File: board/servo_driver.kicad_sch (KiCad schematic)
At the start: 0 parts

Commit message: Hopefully finished schema for pcb
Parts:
- added C2: 33uF, CAP-8*11.5, symbol SCH_Buck Converter_2023-10-10:C_FBF4E86A
- added R10, R11, R12, R13, R14, R15, R16, R17, R18, R19, R20, R21, R22, R7, R8, R9: 220, symbol Device:R
- added R5: 10k, symbol Device:R
- added U5: PCA9685PW, Package_SO:TSSOP-28_4.4x9.7mm_P0.65mm, symbol Driver_LED:PCA9685PW
- added conn_3x1, conn_3x2, conn_3x3, conn_3x4: conn_03x04_Pin, symbol .kicad_sym:conn_03x04_Pin
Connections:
- new net: R5.2, U5.23 (~{OE})
- new net: R11.1, conn_3x2. (9)
- new net: R13.1, conn_3x2. (9)
- new net: R10.1, conn_3x1. (9)
- new net: R21.1, conn_3x4. (9)
- new net: R9.1, conn_3x1. (9)
- new net: R15.1, conn_3x3. (9)
- new net: R18.1, conn_3x3. (9)
- new net: R14.1, conn_3x2. (9)
- new net: R16.1, conn_3x3. (9)
- new net: R17.1, conn_3x3. (9)
- new net: R7.1, conn_3x1. (9)
- new net: R8.1, conn_3x1. (9)
- new net: R22.1, conn_3x4. (9)
- new net: R20.1, conn_3x4. (9)
- new net: R19.1, conn_3x4. (9)
- new net: R12.1, conn_3x2. (9)
- new net +5V: C2.1, U5.1 (A0), U5.24 (A5), U5.28 (VDD), U5.3 (A2), U5.4 (A3), conn_3x1. (9), conn_3x2. (9), conn_3x3. (9)
- new net GND: C2.2, R5.1, U5.2 (A1), U5.25 (EXTCLK), U5.5 (A4), conn_3x1. (9), conn_3x2. (9), conn_3x3. (9), conn_3x4. (9)
- new net PWM0: R14.2, R7.2, U5.6 (LED0)
- new net PWM1: R8.2, U5.7 (LED1)
- new net PWM10: R17.2, U5.17 (LED10)
- new net PWM11: R18.2, U5.18 (LED11)
- new net PWM12: R19.2, U5.19 (LED12)
- new net PWM13: R20.2, U5.20 (LED13)
- new net PWM14: R21.2, U5.21 (LED14)
- new net PWM15: R22.2, U5.22 (LED15)
- new net PWM2: R9.2, U5.8 (LED2)
- new net PWM3: R10.2, U5.9 (LED3)
- new net PWM4: R11.2, U5.10 (LED4)
- new net PWM5: R12.2, U5.11 (LED5)
- new net PWM6: U5.12 (LED6)
- new net PWM7: R13.2, U5.13 (LED7)
- new net PWM8: R15.2, U5.15 (LED8)
- new net PWM9: R16.2, U5.16 (LED9)
- new net SDA: U5.27 (SDA)
- new net SLC: U5.26 (SCL)
- no-connect marks 0 -> 5
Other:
- note added: "PCA9685"
- note added: "Pinout"

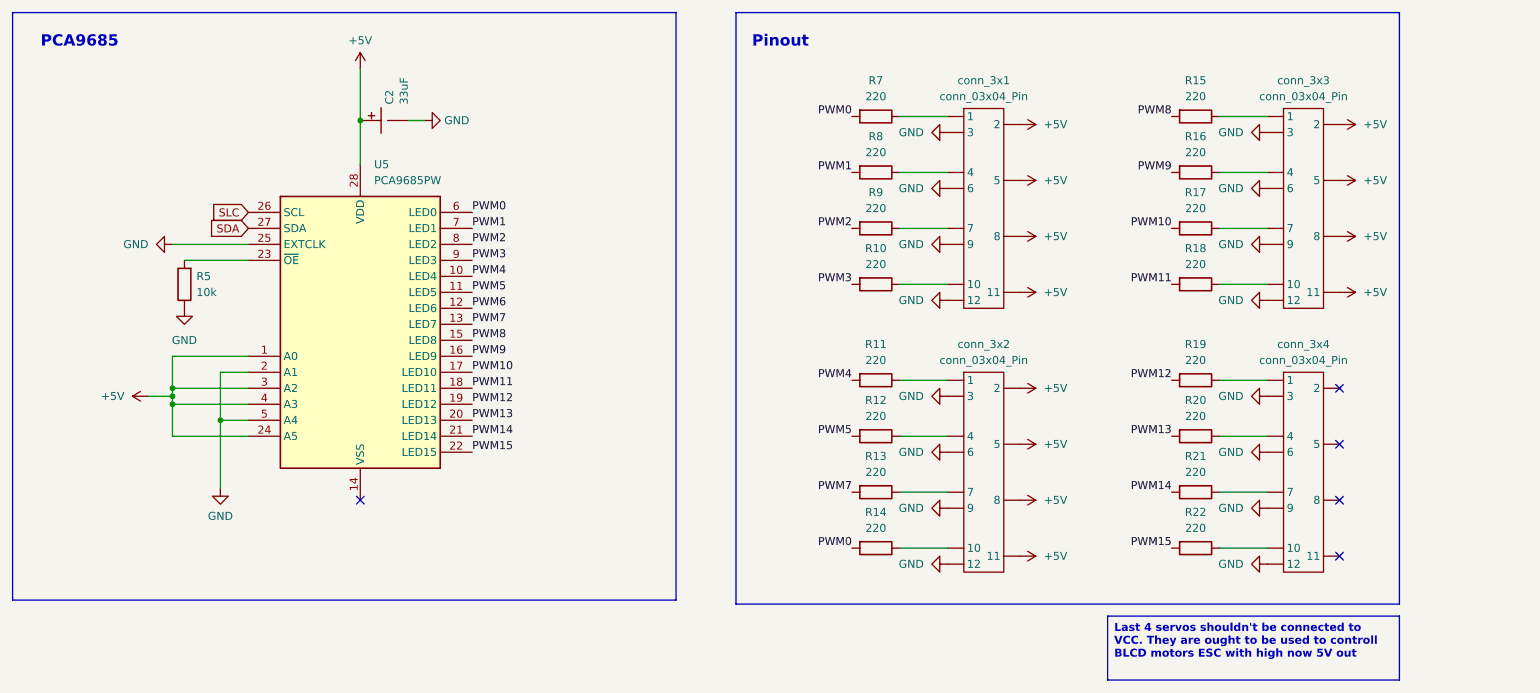
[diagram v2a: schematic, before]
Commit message: Updated schme to comply with electrical rules checker, prepared sensor logic for rewrite
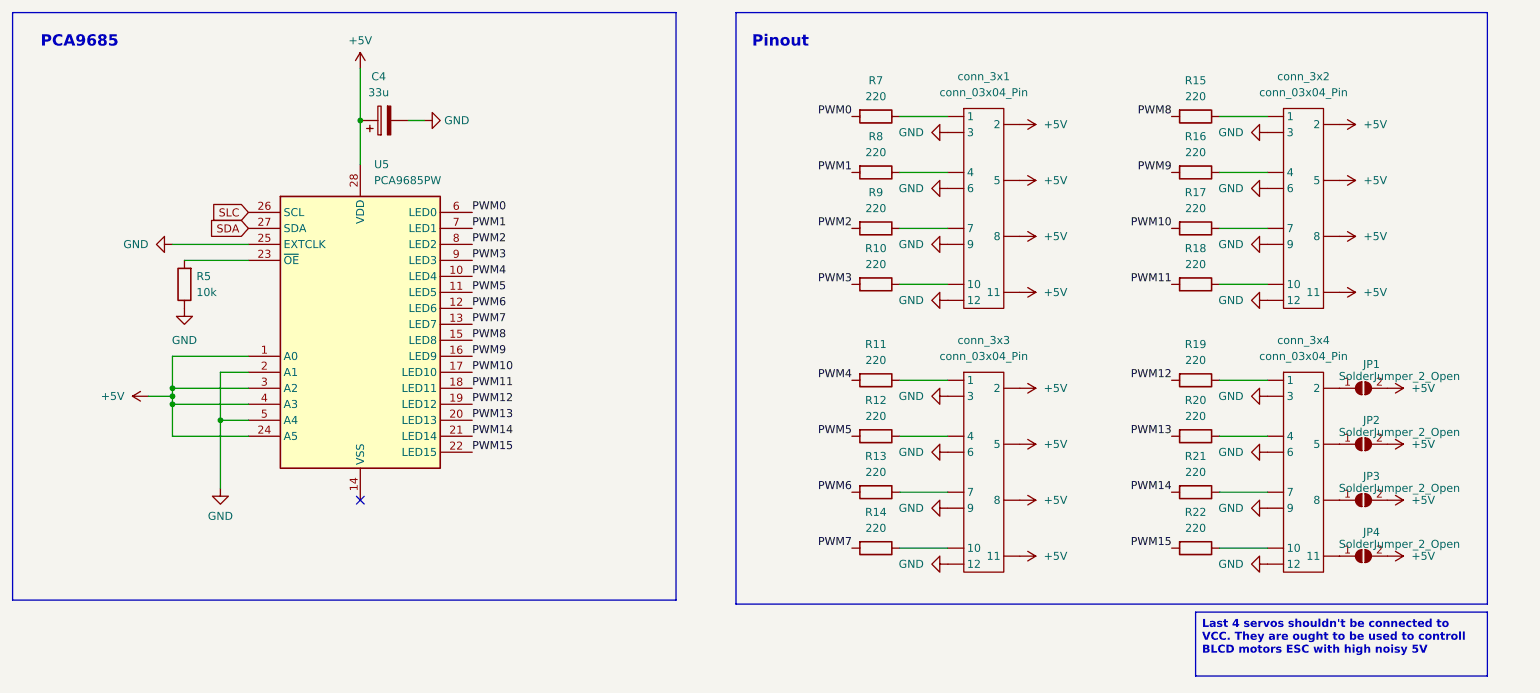
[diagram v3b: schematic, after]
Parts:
- removed C2: 33uF, CAP-8*11.5, symbol SCH_Buck Converter_2023-10-10:C_FBF4E86A
- removed conn_3x1, conn_3x2, conn_3x3, conn_3x4: conn_03x04_Pin, symbol .kicad_sym:conn_03x04_Pin
- added C4: 33u, symbol Device:C_Polarized
- added JP1, JP2, JP3, JP4: SolderJumper_2_Open, Jumper:SolderJumper-2_P1.3mm_Open_Pad1.0x1.5mm, symbol Jumper:SolderJumper_2_Open
- added conn_3x1, conn_3x2, conn_3x3, conn_3x4: conn_03x04_Pin, Custom_Footprints:PinHeader_3x04, symbol Custom_Symbols:conn_03x04_Pin
- R10, R11, R12, R13, R14, R15, R16, R17, R18, R19, R20, R21, R22, R5, R7, R8, R9: footprint (none) -> Resistor_SMD:R_0603_1608Metric
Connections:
- net +5V: now also C4.1, JP1.2 (B), JP2.2 (B), JP3.2 (B), JP4.2 (B), conn_3x1. (9), conn_3x2. (9), conn_3x3. (9)
- net GND: now also C4.2, conn_3x1. (9), conn_3x2. (9), conn_3x3. (9), conn_3x4. (9)
- net PWM0: no longer R14.2
- net PWM6: now also R13.2
- net PWM7: now also R14.2; no longer R13.2
- net at R11.1: now also conn_3x3. (9)
- net at R13.1: now also conn_3x3. (9)
- net at R10.1: now also conn_3x1. (9)
- net at R21.1: now also conn_3x4. (9)
- net at R9.1: now also conn_3x1. (9)
- net at R15.1: now also conn_3x2. (9)
- net at R18.1: now also conn_3x2. (9)
- net at R14.1: now also conn_3x3. (9)
- net at R16.1: now also conn_3x2. (9)
- net at R17.1: now also conn_3x2. (9)
- net at R7.1: now also conn_3x1. (9)
- net at R8.1: now also conn_3x1. (9)
- net at R22.1: now also conn_3x4. (9)
- net at R20.1: now also conn_3x4. (9)
- net at R19.1: now also conn_3x4. (9)
- net at R12.1: now also conn_3x3. (9)
- new net: JP3.1 (A), conn_3x4. (9)
- new net: JP2.1 (A), conn_3x4. (9)
- new net: JP4.1 (A), conn_3x4. (9)
- new net: JP1.1 (A), conn_3x4. (9)
- no-connect marks 5 -> 1

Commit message: More work in reformating drone side of codebase to be semi usable
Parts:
- C4: footprint (none) -> Capacitor_THT:CP_Radial_D8.0mm_P3.50mm
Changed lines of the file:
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@@
       (effects (font (size 1.27 1.27)))
     )
-    (property "Footprint" "" (at 85.725 65.7098 0)
+    (property "Footprint" "Capacitor_THT:CP_Radial_D8.0mm_P3.50mm" (at 85.725 65.7098 0)
       (effects (font (size 1.27 1.27)) hide)
     )

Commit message: Started work on PCB design, more work on rewritting firmware to be semi usable
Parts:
- C4: footprint Capacitor_THT:CP_Radial_D8.0mm_P3.50mm -> Capacitor_THT:CP_Radial_D5.0mm_P2.50mm
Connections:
- net +5V: now also conn_3x1.11, conn_3x1.2, conn_3x1.5, conn_3x1.8, conn_3x2.11, conn_3x2.2, conn_3x2.5, conn_3x2.8, conn_3x3.11, conn_3x3.2, conn_3x3.5, conn_3x3.8; no longer conn_3x1. (9), conn_3x2. (9), conn_3x3. (9)
- net GND: now also conn_3x1.12, conn_3x1.3, conn_3x1.6, conn_3x1.9, conn_3x2.12, conn_3x2.3, conn_3x2.6, conn_3x2.9, conn_3x3.12, conn_3x3.3, conn_3x3.6, conn_3x3.9, conn_3x4.12, conn_3x4.3, conn_3x4.6, conn_3x4.9; no longer conn_3x1. (9), conn_3x2. (9), conn_3x3. (9), conn_3x4. (9)
- net at R11.1: now also conn_3x3.1; no longer conn_3x3. (9)
- net at JP3.1 (A): now also conn_3x4.8; no longer conn_3x4. (9)
- net at R13.1: now also conn_3x3.7; no longer conn_3x3. (9)
- net at R14.1: now also conn_3x3.10; no longer conn_3x3. (9)
- net at R12.1: now also conn_3x3.4; no longer conn_3x3. (9)
- net at R10.1: now also conn_3x1.10; no longer conn_3x1. (9)
- net at R9.1: now also conn_3x1.7; no longer conn_3x1. (9)
- net at R7.1: now also conn_3x1.1; no longer conn_3x1. (9)
- net at R8.1: now also conn_3x1.4; no longer conn_3x1. (9)
- net at JP2.1 (A): now also conn_3x4.5; no longer conn_3x4. (9)
- net at JP4.1 (A): now also conn_3x4.11; no longer conn_3x4. (9)
- net at R21.1: now also conn_3x4.7; no longer conn_3x4. (9)
- net at R15.1: now also conn_3x2.1; no longer conn_3x2. (9)
- net at R18.1: now also conn_3x2.10; no longer conn_3x2. (9)
- net at JP1.1 (A): now also conn_3x4.2; no longer conn_3x4. (9)
- net at R16.1: now also conn_3x2.4; no longer conn_3x2. (9)
- net at R17.1: now also conn_3x2.7; no longer conn_3x2. (9)
- net at R22.1: now also conn_3x4.10; no longer conn_3x4. (9)
- net at R20.1: now also conn_3x4.4; no longer conn_3x4. (9)
- net at R19.1: now also conn_3x4.1; no longer conn_3x4. (9)
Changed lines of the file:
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@@
+    )
+  )
+  (symbol (lib_name "conn_03x04_Pin_1") (lib_id "Custom_Symbols:conn_03x04_Pin") (at 176.53 62.23 0) (unit 1)
+    (in_bom yes) (on_board yes) (dnp no) (fields_autoplaced)
+    (property "Reference" "conn_3x1" (at 177.165 59.69 0)
+      (effects (font (size 1.27 1.27)))
+    )
+    (property "Value" "conn_03x04_Pin" (at 177.165 62.23 0)
+      (effects (font (size 1.27 1.27)))
+    )
+    (property "Footprint" "Custom_Footprints:PinHeader_3x04" (at 176.53 62.23 0)
+      (effects (font (size 1.27 1.27)) hide)
+    )
+    (property "Datasheet" "" (at 176.53 62.23 0)
+      (effects (font (size 1.27 1.27)) hide)
+    )
+    (pin "1")
+    (pin "10")
+    (pin "11")
+    (pin "12")
+    (pin "2")
+    (pin "3")
+    (pin "4")
+    (pin "5")
+    (pin "6")
+    (pin "7")
+    (pin "8")
+    (pin "9")
+    (instances
+      (project "uav_project"
+        (path "/a8bf0924-b264-4c19-8c7e-9c0e131cacba/46d9e855-1ab1-4192-9cab-93e4258e1e2b"
+          (reference "conn_3x1") (unit 1)
+        )
+      )
     )
   )
@@
     )
   )
-  (symbol (lib_id "Custom_Symbols:conn_03x04_Pin") (at 176.53 104.14 0) (unit 1)
-    (in_bom yes) (on_board yes) (dnp no) (fields_autoplaced)
-    (property "Reference" "conn_3x3" (at 177.165 101.6 0)
-      (effects (font (size 1.27 1.27)))
-    )
-    (property "Value" "conn_03x04_Pin" (at 177.165 104.14 0)
-      (effects (font (size 1.27 1.27)))
-    )
-    (property "Footprint" "Custom_Footprints:PinHeader_3x04" (at 176.53 104.14 0)
-      (effects (font (size 1.27 1.27)) hide)
-    )
-    (property "Datasheet" "" (at 176.53 104.14 0)
-      (effects (font (size 1.27 1.27)) hide)
-    )
-    (pin "")
-    (pin "")
-    (pin "")
-    (pin "")
-    (pin "")
-    (pin "")
-    (pin "")
-    (pin "")
-    (pin "")
-    (pin "")
-    (pin "")
-    (pin "")
-    (instances
-      (project "uav_project"
-        (path "/a8bf0924-b264-4c19-8c7e-9c0e131cacba/46d9e855-1ab1-4192-9cab-93e4258e1e2b"
-          (reference "conn_3x3") (unit 1)
-        )
-      )
-    )
-  )
   (symbol (lib_id "power:+5V") (at 233.68 76.2 270) (unit 1)
     (in_bom yes) (on_board yes) (dnp no) (fields_autoplaced)
@@
     )
   )
-  (symbol (lib_id "Custom_Symbols:conn_03x04_Pin") (at 176.53 62.23 0) (unit 1)
-    (in_bom yes) (on_board yes) (dnp no) (fields_autoplaced)
-    (property "Reference" "conn_3x1" (at 177.165 59.69 0)
-      (effects (font (size 1.27 1.27)))
-    )
-    (property "Value" "conn_03x04_Pin" (at 177.165 62.23 0)
-      (effects (font (size 1.27 1.27)))
-    )
-    (property "Footprint" "Custom_Footprints:PinHeader_3x04" (at 176.53 62.23 0)
-      (effects (font (size 1.27 1.27)) hide)
-    )
-    (property "Datasheet" "" (at 176.53 62.23 0)
-      (effects (font (size 1.27 1.27)) hide)
-    )
-    (pin "")
-    (pin "")
-    (pin "")
-    (pin "")
-    (pin "")
-    (pin "")
-    (pin "")
-    (pin "")
-    (pin "")
-    (pin "")
-    (pin "")
-    (pin "")
-    (instances
-      (project "uav_project"
-        (path "/a8bf0924-b264-4c19-8c7e-9c0e131cacba/46d9e855-1ab1-4192-9cab-93e4258e1e2b"
-          (reference "conn_3x1") (unit 1)
+  (symbol (lib_name "conn_03x04_Pin_1") (lib_id "Custom_Symbols:conn_03x04_Pin") (at 227.33 62.23 0) (unit 1)
+    (in_bom yes) (on_board yes) (dnp no) (fields_autoplaced)
+    (property "Reference" "conn_3x2" (at 227.965 59.69 0)
+      (effects (font (size 1.27 1.27)))
+    )
+    (property "Value" "conn_03x04_Pin" (at 227.965 62.23 0)
+      (effects (font (size 1.27 1.27)))
+    )
+    (property "Footprint" "Custom_Footprints:PinHeader_3x04" (at 227.33 62.23 0)
+      (effects (font (size 1.27 1.27)) hide)
+    )
+    (property "Datasheet" "" (at 227.33 62.23 0)
+      (effects (font (size 1.27 1.27)) hide)
+    )
+    (pin "1")
+    (pin "10")
+    (pin "11")
+    (pin "12")
+    (pin "2")
+    (pin "3")
+    (pin "4")
+    (pin "5")
+    (pin "6")
+    (pin "7")
+    (pin "8")
+    (pin "9")
+    (instances
+      (project "uav_project"
+        (path "/a8bf0924-b264-4c19-8c7e-9c0e131cacba/46d9e855-1ab1-4192-9cab-93e4258e1e2b"
+          (reference "conn_3x2") (unit 1)
         )
       )
@@
     )
   )
+  (symbol (lib_name "conn_03x04_Pin_1") (lib_id "Custom_Symbols:conn_03x04_Pin") (at 227.33 104.14 0) (unit 1)
+    (in_bom yes) (on_board yes) (dnp no) (fields_autoplaced)
+    (property "Reference" "conn_3x4" (at 227.965 101.6 0)
+      (effects (font (size 1.27 1.27)))
+    )
+    (property "Value" "conn_03x04_Pin" (at 227.965 104.14 0)
+      (effects (font (size 1.27 1.27)))
+    )
+    (property "Footprint" "Custom_Footprints:PinHeader_3x04" (at 227.33 104.14 0)
+      (effects (font (size 1.27 1.27)) hide)
+    )
+    (property "Datasheet" "" (at 227.33 104.14 0)
+      (effects (font (size 1.27 1.27)) hide)
+    )
+    (pin "1")
+    (pin "10")
+    (pin "11")
+    (pin "12")
+    (pin "2")
+    (pin "3")
+    (pin "4")
+    (pin "5")
+    (pin "6")
+    (pin "7")
+    (pin "8")
+    (pin "9")
+    (instances
+      (project "uav_project"
+        (path "/a8bf0924-b264-4c19-8c7e-9c0e131cacba/46d9e855-1ab1-4192-9cab-93e4258e1e2b"
+          (reference "conn_3x4") (unit 1)
+        )
+      )
+    )
+  )
   (symbol (lib_id "Device:R") (at 210.82 66.04 270) (unit 1)
     (in_bom yes) (on_board yes) (dnp no) (fields_autoplaced)
@@
     )
   )
+  (symbol (lib_name "conn_03x04_Pin_1") (lib_id "Custom_Symbols:conn_03x04_Pin") (at 176.53 104.14 0) (unit 1)
+    (in_bom yes) (on_board yes) (dnp no) (fields_autoplaced)
+    (property "Reference" "conn_3x3" (at 177.165 101.6 0)
+      (effects (font (size 1.27 1.27)))
+    )
+    (property "Value" "conn_03x04_Pin" (at 177.165 104.14 0)
+      (effects (font (size 1.27 1.27)))
+    )
+    (property "Footprint" "Custom_Footprints:PinHeader_3x04" (at 176.53 104.14 0)
+      (effects (font (size 1.27 1.27)) hide)
+    )
+    (property "Datasheet" "" (at 176.53 104.14 0)
+      (effects (font (size 1.27 1.27)) hide)
+    )
+    (pin "1")
+    (pin "10")
+    (pin "11")
+    (pin "12")
+    (pin "2")
+    (pin "3")
+    (pin "4")
+    (pin "5")
+    (pin "6")
+    (pin "7")
+    (pin "8")
+    (pin "9")
+    (instances
+      (project "uav_project"
+        (path "/a8bf0924-b264-4c19-8c7e-9c0e131cacba/46d9e855-1ab1-4192-9cab-93e4258e1e2b"
+          (reference "conn_3x3") (unit 1)
+        )
+      )
+    )
+  )
   (symbol (lib_id "Device:R") (at 160.02 134.62 270) (unit 1)
     (in_bom yes) (on_board yes) (dnp no) (fields_autoplaced)
@@
     )
   )
-  (symbol (lib_id "Custom_Symbols:conn_03x04_Pin") (at 227.33 62.23 0) (unit 1)
-    (in_bom yes) (on_board yes) (dnp no) (fields_autoplaced)
-    (property "Reference" "conn_3x2" (at 227.965 59.69 0)
-      (effects (font (size 1.27 1.27)))
-    )
-    (property "Value" "conn_03x04_Pin" (at 227.965 62.23 0)
-      (effects (font (size 1.27 1.27)))
-    )
-    (property "Footprint" "Custom_Footprints:PinHeader_3x04" (at 227.33 62.23 0)
-      (effects (font (size 1.27 1.27)) hide)
-    )
-    (property "Datasheet" "" (at 227.33 62.23 0)
-      (effects (font (size 1.27 1.27)) hide)
-    )
-    (pin "")
-    (pin "")
-    (pin "")
-    (pin "")
-    (pin "")
-    (pin "")
-    (pin "")
-    (pin "")
-    (pin "")
-    (pin "")
-    (pin "")
-    (pin "")
-    (instances
-      (project "uav_project"
-        (path "/a8bf0924-b264-4c19-8c7e-9c0e131cacba/46d9e855-1ab1-4192-9cab-93e4258e1e2b"
-          (reference "conn_3x2") (unit 1)
-        )
-      )
-    )
-  )
   (symbol (lib_id "power:+5V") (at 44.45 110.49 90) (unit 1)
     (in_bom yes) (on_board yes) (dnp no) (fields_autoplaced)
@@
       (effects (font (size 1.27 1.27)))
     )
-    (property "Footprint" "Capacitor_THT:CP_Radial_D8.0mm_P3.50mm" (at 85.725 65.7098 0)
+    (property "Footprint" "Capacitor_THT:CP_Radial_D5.0mm_P2.50mm" (at 85.725 65.7098 0)
       (effects (font (size 1.27 1.27)) hide)
     )
@@
         )
       )
-    )
-  )
-  (symbol (lib_id "Custom_Symbols:conn_03x04_Pin") (at 227.33 104.14 0) (unit 1)
-    (in_bom yes) (on_board yes) (dnp no) (fields_autoplaced)
-    (property "Reference" "conn_3x4" (at 227.965 101.6 0)
-      (effects (font (size 1.27 1.27)))
-    )
-    (property "Value" "conn_03x04_Pin" (at 227.965 104.14 0)
-      (effects (font (size 1.27 1.27)))
-    )
-    (property "Footprint" "Custom_Footprints:PinHeader_3x04" (at 227.33 104.14 0)
-      (effects (font (size 1.27 1.27)) hide)
-    )
-    (property "Datasheet" "" (at 227.33 104.14 0)
-      (effects (font (size 1.27 1.27)) hide)
-    )
-    (pin "")
-    (pin "")
-    (pin "")
-    (pin "")
-    (pin "")
-    (pin "")
-    (pin "")
-    (pin "")
-    (pin "")
-    (pin "")
-    (pin "")
-    (pin "")
-    (instances
-      (project "uav_project"
-        (path "/a8bf0924-b264-4c19-8c7e-9c0e131cacba/46d9e855-1ab1-4192-9cab-93e4258e1e2b"
-          (reference "conn_3x4") (unit 1)
-        )
-      )
